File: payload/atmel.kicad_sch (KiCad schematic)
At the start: 12 parts, among them J501 Conn_01x02, J502 AVR-ISP-6, U501 ATmega328-P, Y501 ECS-100-S-20A-TR

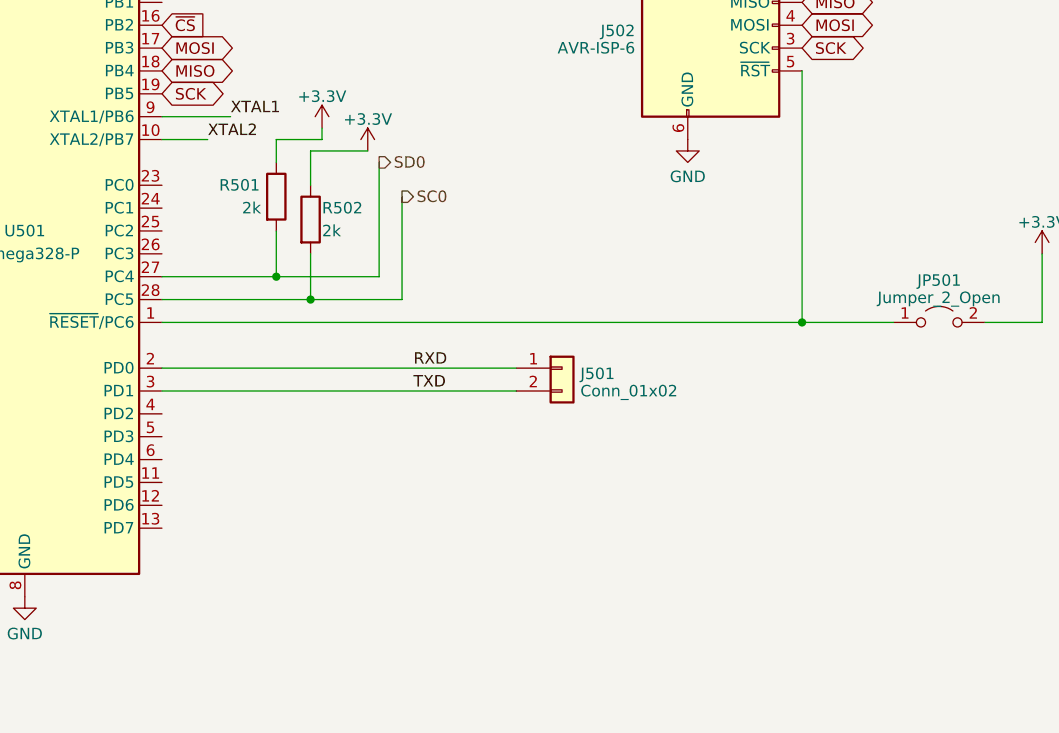
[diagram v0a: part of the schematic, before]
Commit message: added LEDs
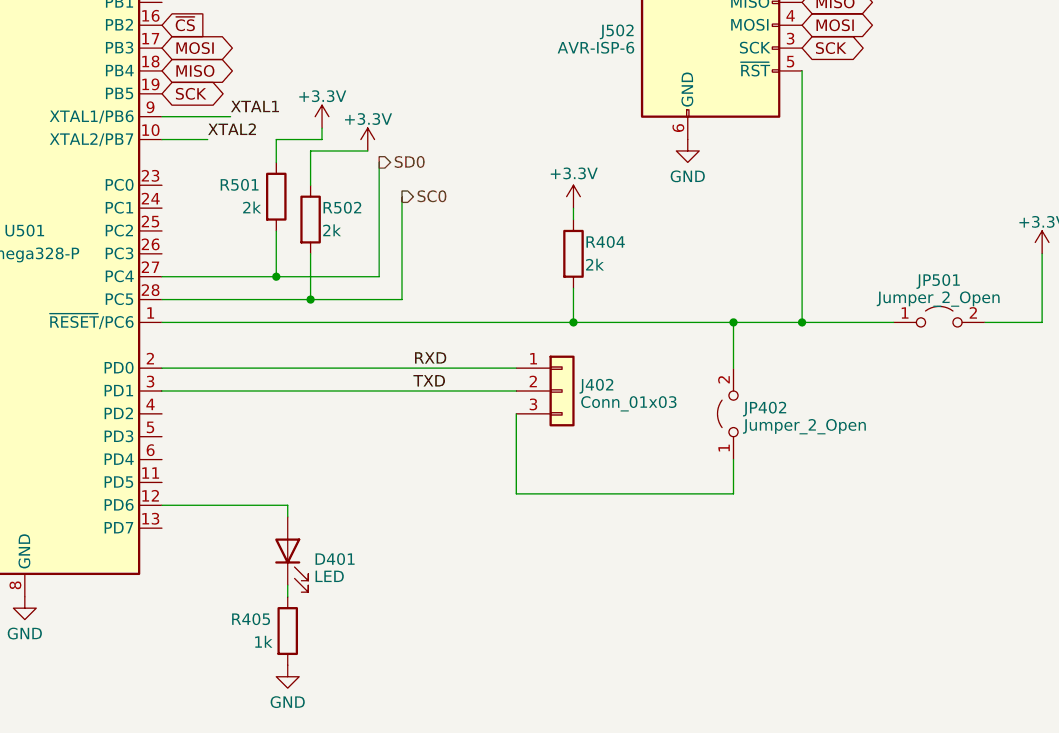
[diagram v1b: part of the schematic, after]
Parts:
- removed J501: Conn_01x02, Connector_Phoenix_MC:PhoenixContact_MCV_1,5_2-G-3.81_1x02_P3.81mm_Vertical, symbol Connector_Generic:Conn_01x02
- added D401: LED, LED_SMD:LED_0402_1005Metric_Pad0.77x0.64mm_HandSolder, symbol Device:LED
- added J402: Conn_01x03, Connector_PinHeader_2.00mm:PinHeader_1x03_P2.00mm_Vertical, symbol Connector_Generic:Conn_01x03
- added JP402: Jumper_2_Open, Jumper:SolderJumper-2_P1.3mm_Open_Pad1.0x1.5mm, symbol Jumper:Jumper_2_Open
- added R404: 2k, Capacitor_SMD:C_0603_1608Metric_Pad1.08x0.95mm_HandSolder, symbol Device:R
- added R405: 1k, Capacitor_SMD:C_0603_1608Metric_Pad1.08x0.95mm_HandSolder, symbol Device:R
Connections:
- net +3.3V: now also R404.1
- net GND: now also R405.2
- net RXD: now also J402.1 (Pin_1)
- net TXD: now also J402.2 (Pin_2)
- net at J502.5 (~{RST}), JP501.1 (A), U501.1 (~{RESET}/PC6): now also JP402.2 (B), R404.2
- net at U501.12 (PD6): now also D401.2 (A)
- new net: J402.3 (Pin_3), JP402.1 (A)
- new net: D401.1 (K), R405.1

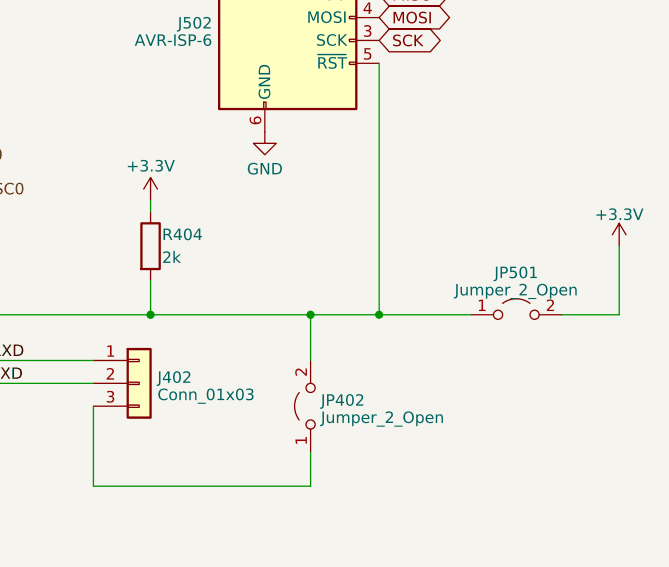
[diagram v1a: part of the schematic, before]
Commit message: added TPs
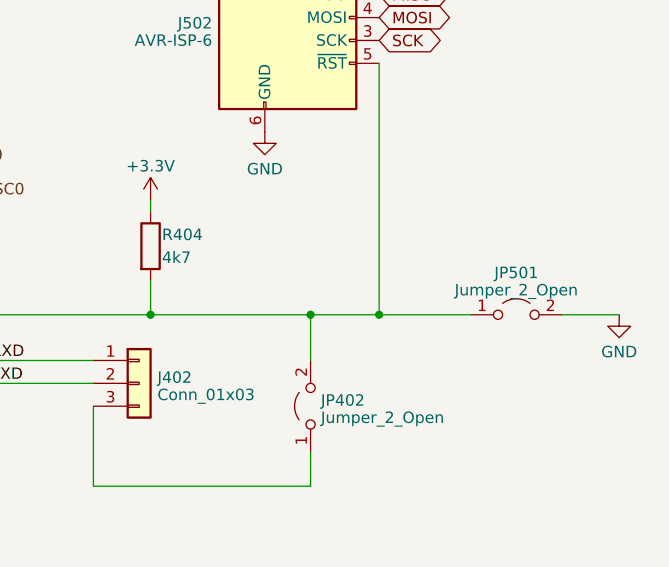
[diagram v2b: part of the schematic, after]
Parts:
- R404: value 2k -> 4k7
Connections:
- net +3.3V: no longer JP501.2 (B)
- net GND: now also JP501.2 (B)
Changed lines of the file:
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@@
-    (stroke (width 0) (type default))
-  )
-  (wire (pts (xy 251.46 106.68) (xy 251.46 99.06))
     (stroke (width 0) (type default))
   )
@@
     )
   )
+  (symbol (lib_id "power:GND") (at 251.46 106.68 0) (unit 1)
+    (in_bom yes) (on_board yes) (dnp no) (fields_autoplaced)
+    (property "Reference" "#PWR0417" (at 251.46 113.03 0)
+      (effects (font (size 1.27 1.27)) hide)
+    )
+    (property "Value" "GND" (at 251.46 110.8155 0)
+      (effects (font (size 1.27 1.27)))
+    )
+    (property "Footprint" "" (at 251.46 106.68 0)
+      (effects (font (size 1.27 1.27)) hide)
+    )
+    (property "Datasheet" "" (at 251.46 106.68 0)
+      (effects (font (size 1.27 1.27)) hide)
+    )
+    (pin "1")
+    (instances
+      (project "payload"
+        (path "/0a419cb9-bfa0-442e-8f67-9cc2093d7c87/dea4f99a-06bc-4245-ba10-4d6e21532046"
+          (reference "#PWR0417") (unit 1)
+        )
+      )
+      (project "electrical-power-system"
+        (path "/5987de0a-a772-40e3-9e89-af52950d87bb/a29c39c3-f61d-41a4-b663-9cd24fc958f0"
+          (reference "#PWR0408") (unit 1)
+        )
+      )
+    )
+  )
   (symbol (lib_id "power:+3.3V") (at 120.65 44.45 0) (unit 1)
     (in_bom yes) (on_board yes) (dnp no) (fields_autoplaced)
@@
       (effects (font (size 1.27 1.27)) (justify left))
     )
-    (property "Value" "2k" (at 200.66 100.33 0)
+    (property "Value" "4k7" (at 200.66 100.33 0)
       (effects (font (size 1.27 1.27)) (justify left))
     )
@@
         )
       )
-    )
-  )
-  (symbol (lib_id "power:+3.3V") (at 251.46 99.06 0) (unit 1)
-    (in_bom yes) (on_board yes) (dnp no) (fields_autoplaced)
-    (property "Reference" "#PWR0102" (at 251.46 102.87 0)
-      (effects (font (size 1.27 1.27)) hide)
-    )
-    (property "Value" "+3.3V" (at 251.46 95.5581 0)
-      (effects (font (size 1.27 1.27)))
-    )
-    (property "Footprint" "" (at 251.46 99.06 0)
-      (effects (font (size 1.27 1.27)) hide)
-    )
-    (property "Datasheet" "" (at 251.46 99.06 0)
-      (effects (font (size 1.27 1.27)) hide)
-    )
-    (pin "1")
-    (instances
-      (project "payload"
-        (path "/0a419cb9-bfa0-442e-8f67-9cc2093d7c87"
-          (reference "#PWR0102") (unit 1)
-        )
-        (path "/0a419cb9-bfa0-442e-8f67-9cc2093d7c87/dea4f99a-06bc-4245-ba10-4d6e21532046"
-          (reference "#PWR0507") (unit 1)
-        )
-      )
-      (project "electrical-power-system"
-        (path "/5987de0a-a772-40e3-9e89-af52950d87bb"
-          (reference "#PWR0119") (unit 1)
-        )
-      )
